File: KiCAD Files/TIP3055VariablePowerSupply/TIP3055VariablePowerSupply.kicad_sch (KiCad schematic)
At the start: 16 parts, among them J1 Barrel_Jack_Switch, J2 VOUT, Q1 BD139, Q2 MPSA92, Q3 PN2222A, Q4 TIP3055

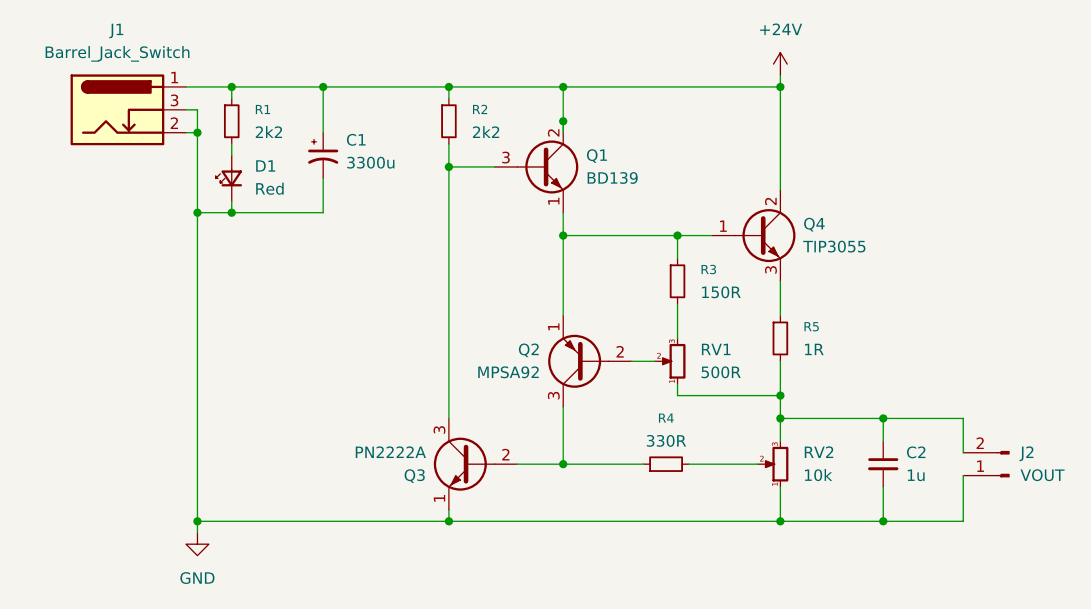
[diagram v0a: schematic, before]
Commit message: Updated Schematic Diagram & Assigned Footprints
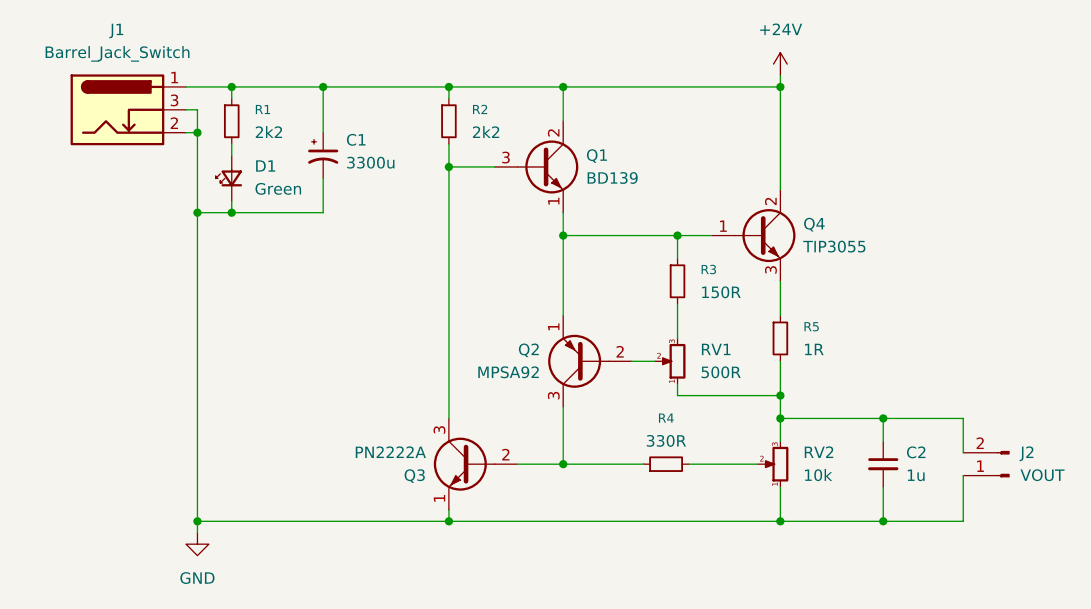
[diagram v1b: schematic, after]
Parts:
- C1: footprint (none) -> Capacitor_THT:CP_Radial_D16.0mm_P7.50mm
- C2: footprint (none) -> Capacitor_THT:CP_Radial_D5.0mm_P2.00mm
- D1: value Red -> Green; footprint (none) -> LED_THT:LED_D5.0mm
- J1: footprint (none) -> Connector_BarrelJack:BarrelJack_Kycon_KLDX-0202-xC_Horizontal
- J2: footprint (none) -> TerminalBlock:TerminalBlock_MaiXu_MX126-5.0-02P_1x02_P5.00mm
- R1, R2: footprint (none) -> Resistor_THT:R_Axial_DIN0309_L9.0mm_D3.2mm_P15.24mm_Horizontal
- R3, R4: footprint (none) -> Resistor_THT:R_Axial_DIN0207_L6.3mm_D2.5mm_P10.16mm_Horizontal
- R5: footprint (none) -> Resistor_THT:R_Axial_Power_L20.0mm_W6.4mm_P25.40mm
- RV1, RV2: footprint (none) -> Potentiometer_THT:Potentiometer_Alps_RK09Y11_Single_Horizontal

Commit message: Updated PCB Design
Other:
- company: (none) -> Halmstad University
- title: (none) -> TIP3055 Variable DC Power Supply (Redesign by Mbeche JP)
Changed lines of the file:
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@@
 	(generator_version "9.0")
 	(paper "A4")
+	(title_block
+		(title "TIP3055 Variable DC Power Supply (Redesign by Mbeche JP)")
+		(date "2025-04-21")
+		(rev "1.0")
+		(company "Halmstad University")
+	)
 	(junction
 		(at 170.18 73.66)
